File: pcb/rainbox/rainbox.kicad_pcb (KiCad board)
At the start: 2 copper layers, 60 x 45 mm, 35 parts, among them J1 USB_C_Receptacle_USB2.0_14P, J2 Conn_01x04_Pin, J3 Conn_01x02_Pin, J4 Conn_01x02_Socket, SW1 SW_Push, SW2 SW_Push, U1 ESP32-S3-WROOM-2, U10 USBLC6-2P6, U2 LM3940IMPX-3.3/NOPB, U3 ESC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

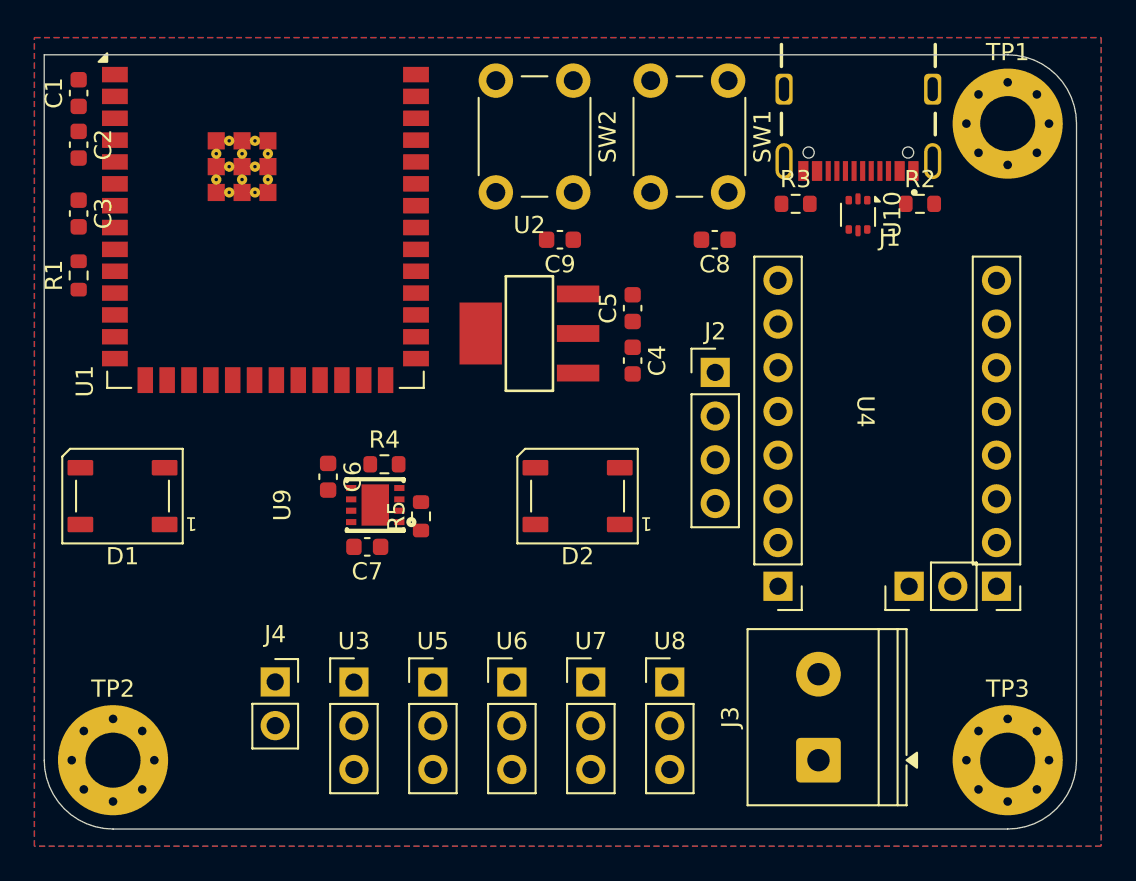
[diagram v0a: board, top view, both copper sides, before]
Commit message: replace esc controller with dc motor ic
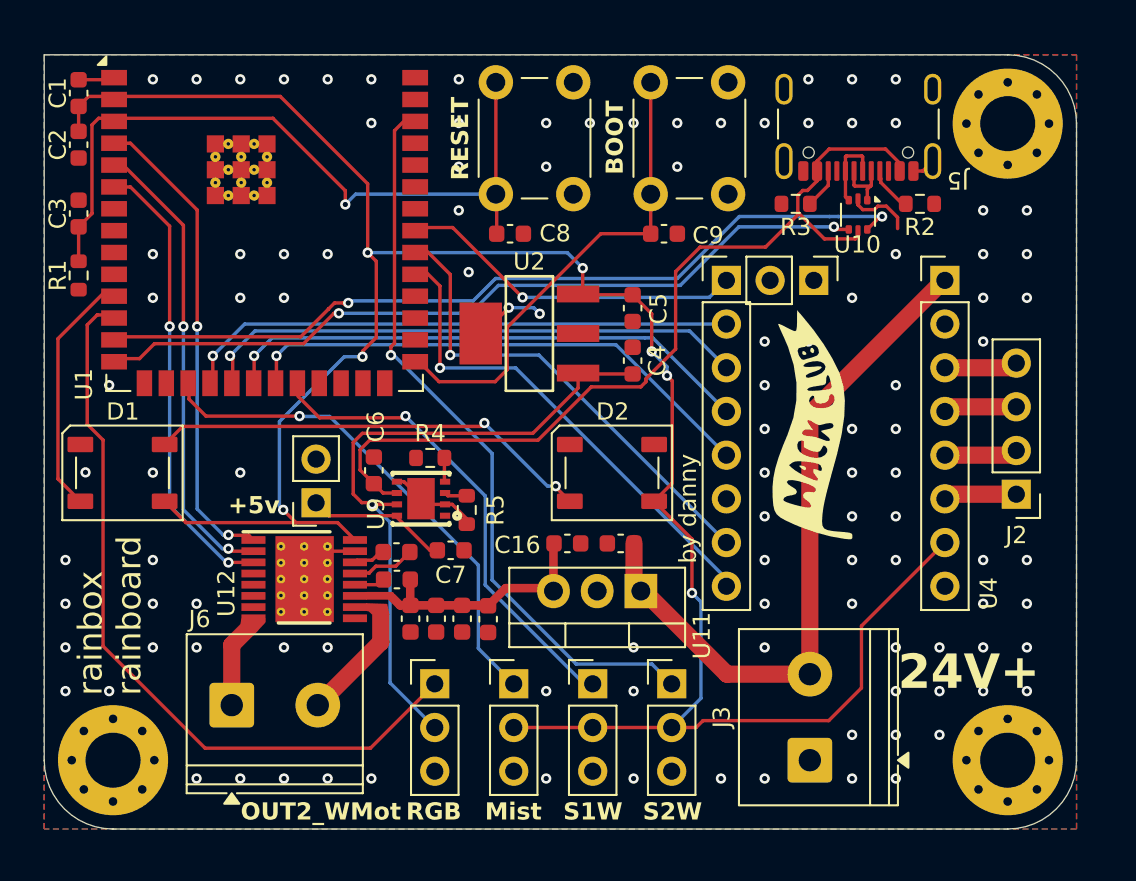
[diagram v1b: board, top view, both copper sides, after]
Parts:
- removed J1: USB_C_Receptacle_USB2.0_14P, Snapeda:USB4105-GF-A_GCT_USB4105-GF-A
- removed U3: ESC, Connector_PinHeader_2.54mm:PinHeader_1x03_P2.54mm_Vertical
- added C10: 22nF, Capacitor_SMD:C_0603_1608Metric, F.Cu at (140.5, 113.9)
- added C11: 220nF, Capacitor_SMD:C_0603_1608Metric, F.Cu at (140.5, 115.5)
- added C12: 0.1uF, Capacitor_SMD:C_0603_1608Metric, F.Cu at (145.8, 117.8)
- added C13: 0.1uF, Capacitor_SMD:C_0603_1608Metric, F.Cu at (144.3, 117.8)
- added C14: 4.7uF, Capacitor_SMD:C_0603_1608Metric, F.Cu at (142.8, 117.8)
- added C15: 4.7uF, Capacitor_SMD:C_0603_1608Metric, F.Cu at (141.3, 117.8)
- added C16: 0.1uF, Capacitor_SMD:C_0603_1608Metric, F.Cu at (150.4, 113.4)
- added C17: 220nF, Capacitor_SMD:C_0603_1608Metric, F.Cu at (153.5, 113.4)
- added G***: LOGO, 1_udu_lib:hackclub, F.Cu at (164.9, 106.7)
- added G***: LOGO, 1_udu_lib:hackclub, B.Cu at (164.6, 107.1)
- added J5: USB4105, Connector_USB:USB_C_Receptacle_GCT_USB4105-xx-A_16P_TopMnt_Horizontal, F.Cu at (167.3, 88.1)
- added J6: Conn_01x02_Socket, TerminalBlock_Phoenix:TerminalBlock_Phoenix_PT-1,5-2-5.0-H_1x02_P5.00mm_Horizontal, F.Cu at (130.9, 122.8)
- added U11: LM7812_TO220, Package_TO_SOT_THT:TO-220-3_Vertical, F.Cu at (154.7, 116.2)
- added U12: DRV8874PWPR, 1_udu_lib:PWP0016J_N, F.Cu at (135.1, 115.5)
- moved J2 18.9 mm to (176.5, 110.5), turned to 180 degrees
- moved SW1 15.0 mm to (146.2, 93.1), turned to 90 degrees
- moved C8 11.9 mm to (147.1, 95.4), turned to 0 degrees
- moved J4 10.7 mm to (135.8, 111.0), turned to 180 degrees
- moved U5 9.29 mm to (151.9, 121.6)
- moved U6 9.29 mm to (156.5, 121.6)
- moved U7 9.07 mm to (142.7, 121.6)
- moved U8 9.07 mm to (147.3, 121.6)
- moved SW2 7.99 mm to (155.2, 93.1), turned to 90 degrees
- moved U4 6.09 mm to (164.7, 108.3), turned to 0 degrees
- moved C9 6.06 mm to (156.0, 95.4), turned to 0 degrees
- moved C7 4.85 mm to (143.6, 113.8)
- moved C6 2.69 mm to (139.2, 109.2)
- moved R5 2.69 mm to (144.6, 111.5)
- moved U9 2.69 mm to (141.9, 110.8)
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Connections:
- net Net-(J3-Pin_2) renamed +24V
- U1 pad 22: unconnected-(U1-IO14-Pad22) -> S1Water
- U1 pad 31: unconnected-(U1-IO38-Pad31) -> DIR
- U1 pad 32: unconnected-(U1-MTCK/IO39-Pad32) -> STEP
- U1 pad 33: unconnected-(U1-MTDO/IO40-Pad33) -> ENABLE
- U1 pad 38: S1Water -> S2Water
- U1 pad 39: ESC_PWM -> unconnected-(U1-IO1-Pad39)
- U1 pad 4: ENABLE -> EN_IN1
- U1 pad 5: STEP -> PH_IN2
- U1 pad 6: DIR -> SLEEP_N
- U1 pad 7: S2Water -> unconnected-(U1-IO7-Pad7)
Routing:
- net +3.3V: track 0.00 -> 133.5 mm, vias 0 -> 7
- net 5V_VBUS: track 0.00 -> 52.1 mm
- net D-: track 0.00 -> 48.7 mm, vias 0 -> 2
- net D+: track 0.00 -> 45.9 mm, vias 0 -> 2
- net RGB: track 0.00 -> 44.2 mm
- net EN_RESET: track 0.00 -> 43.5 mm, vias 0 -> 1
- net S2Water: track 0.00 -> 43.2 mm, vias 0 -> 1
- net +24V: track 0.00 -> 40.8 mm
- net +5V: track 0.00 -> 38.7 mm, vias 0 -> 1
- net MOSI: track 0.00 -> 32.1 mm, vias 0 -> 1
- net SPI_CLK: track 0.00 -> 31.8 mm, vias 0 -> 1
- net CS: track 0.00 -> 31.1 mm, vias 0 -> 1
- net MISO: track 0.00 -> 30.5 mm, vias 0 -> 1
- net Mist: track 0.00 -> 29.7 mm, vias 0 -> 1
- net DIR: track 0.00 -> 28.7 mm, vias 0 -> 1
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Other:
- board text added: "+5v"
- board text added: "24V+"
- board text added: "BOOT"
- board text added: "Mist"
- board text added: "OUT2_WMot"
- board text added: "RESET"
- board text added: "RGB"
- board text added: "S1W"
- board text added: "S2W"
- board text added: "by danny"
- board text added: "rainbox rainboard"

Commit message: pcb additions, readme, md stuff
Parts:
- C5: value 33uF -> 47uF
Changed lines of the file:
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@@
 			)
 		)
-		(property "Value" "33uF"
+		(property "Value" "47uF"
 			(at 0 1.43 90)
 			(layer "F.Fab")

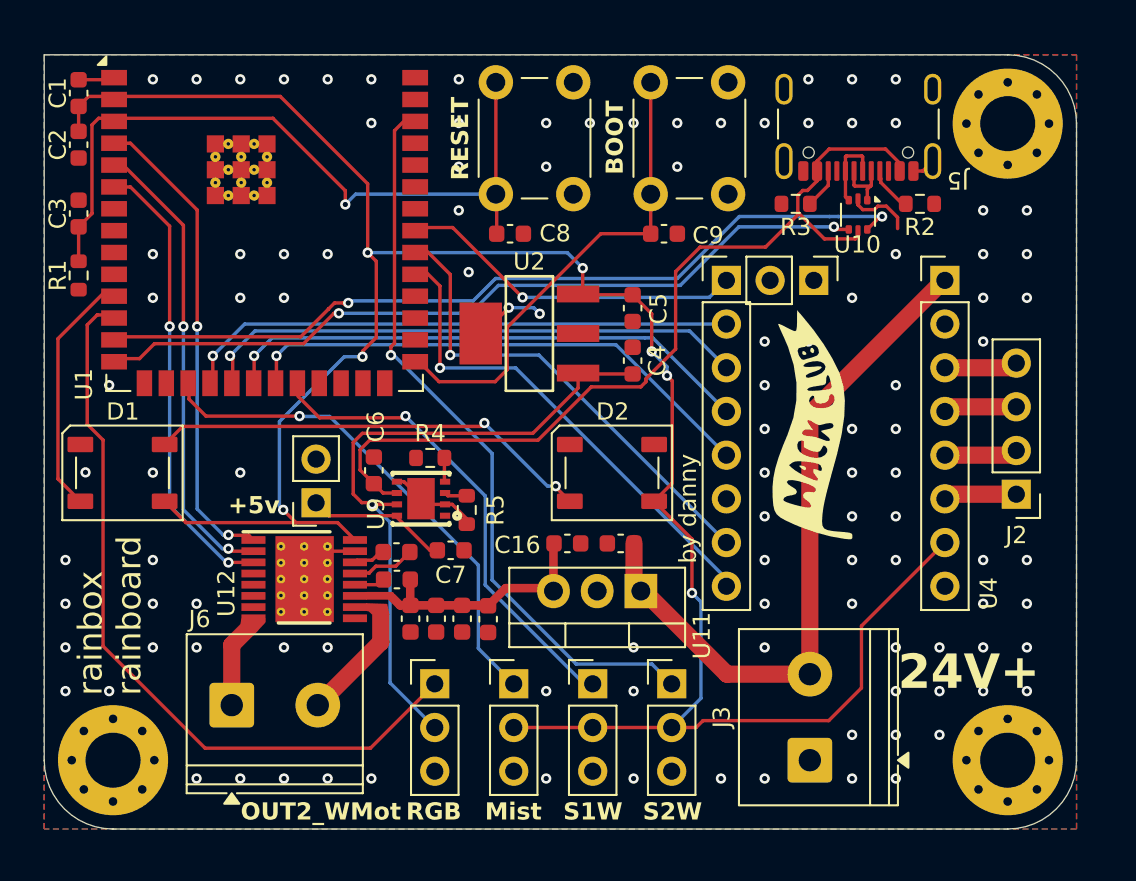
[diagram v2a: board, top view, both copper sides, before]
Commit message: add prototype firmware + fix pcb
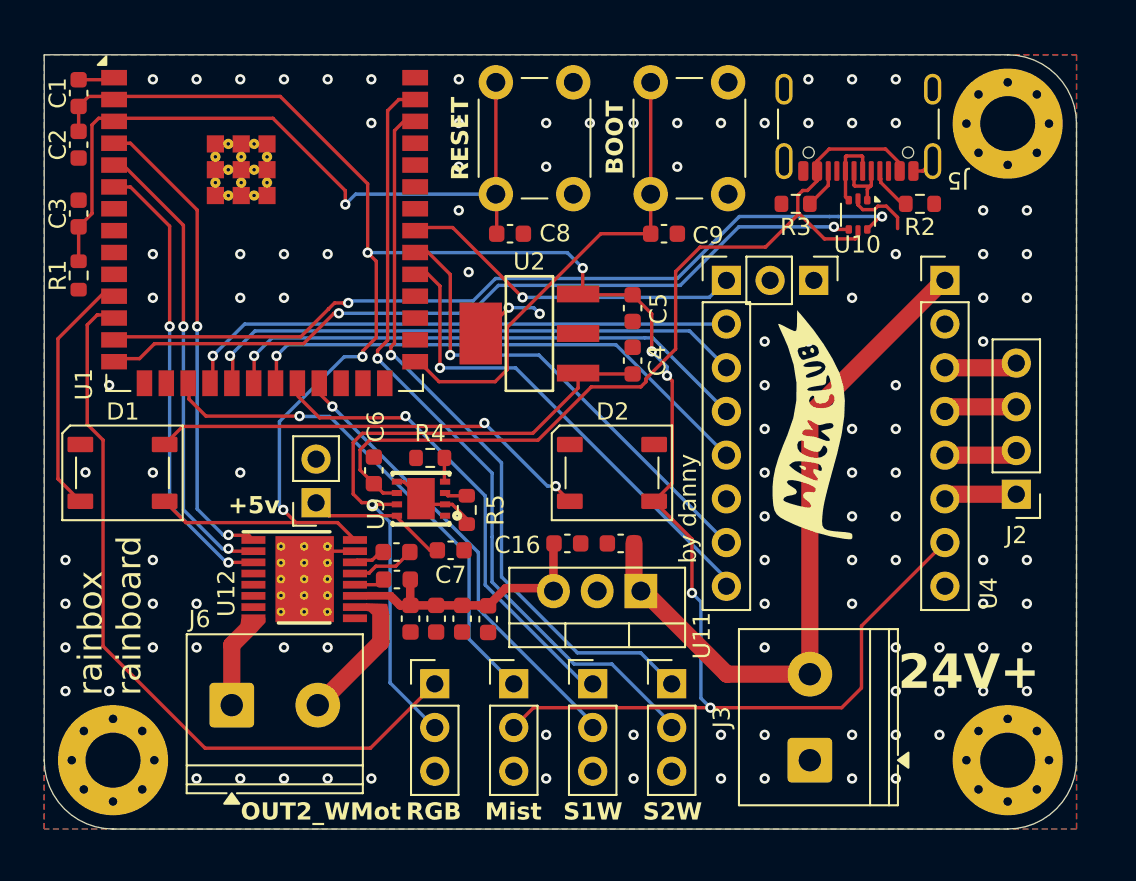
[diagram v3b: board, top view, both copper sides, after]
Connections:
- U1 pad 23: unconnected-(U1-IO21-Pad23) -> S1Power
- U1 pad 39: unconnected-(U1-IO1-Pad39) -> S2Power
- U5 pad 2: +3.3V -> S1Power
- U6 pad 2: +3.3V -> S2Power
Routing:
- net S2Power: track 0.00 -> 46.3 mm, vias 0 -> 1
- net S1Power: track 0.00 -> 26.6 mm, vias 0 -> 1
- net +3.3V: track 133.5 -> 131.9 mm, vias 7 -> 8
- net GND: vias 108 -> 109
